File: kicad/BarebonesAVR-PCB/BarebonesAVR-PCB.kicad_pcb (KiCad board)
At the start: 2 copper layers, 49 x 24.9 mm, 14 parts, among them IC1 ATMEGA328-A, P1 ISP6PIN, P2 CONN_FTDI_AVR, SW1 SW-PUSH-RND-SMALL, Y1 8 MHz

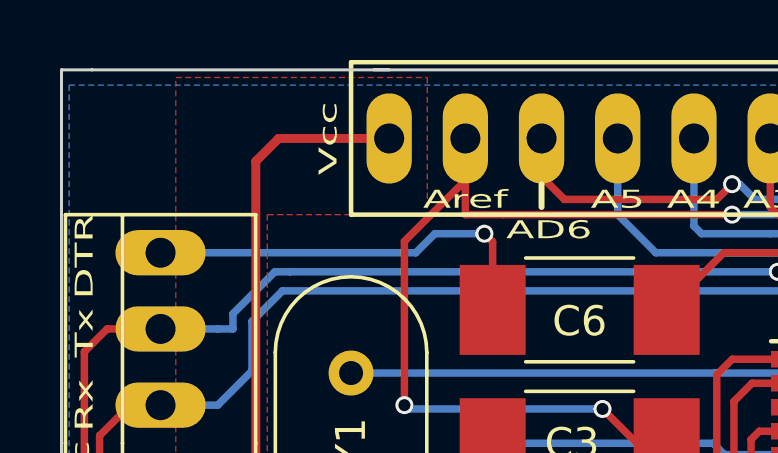
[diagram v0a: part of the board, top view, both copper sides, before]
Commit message: Changed VCC lable to 3.3V
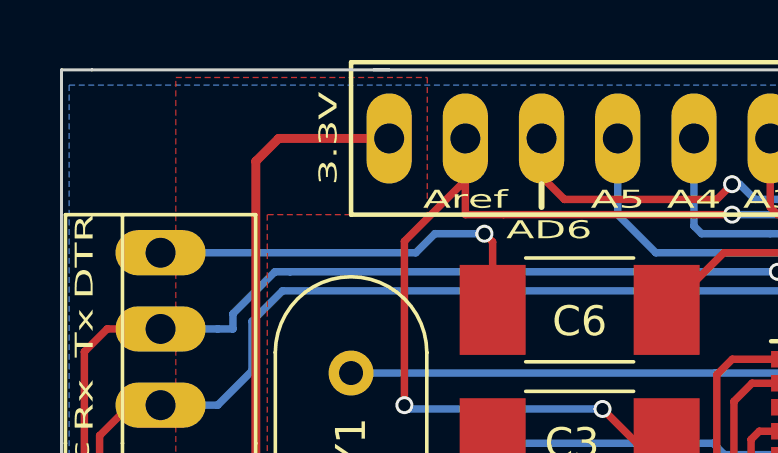
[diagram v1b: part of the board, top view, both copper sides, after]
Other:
- board text added: "3.3V"
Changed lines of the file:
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@@
     (links 55)
     (no_connects 0)
-    (area 126.187999 104.343999 175.310001 129.336001)
+    (area 125.794999 101.795 176.625 131.985)
     (thickness 1.6)
     (drawings 51)
@@
     (effects (font (size 0.6 1) (thickness 0.15)))
   )
-  (gr_text Vcc (at 135.128 106.68 90) (layer F.SilkS)
-    (effects (font (size 0.6 1) (thickness 0.15)))
-  )
+  (gr_text 3.3V (at 135.128 106.68 90) (layer F.SilkS)
+    (effects (font (size 0.6 1) (thickness 0.15)))
+  )
